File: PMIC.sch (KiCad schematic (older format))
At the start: 44 parts

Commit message: started working on implementing i.MX7 core into base schematic
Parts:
- removed D?: 1N5819HW-7-F, symbol SCHOTTKY
- removed U?: PF3000, symbol PF3000
- added BT?: Battery_Cell, symbol Battery_Cell
- added C? (x12): 22u, symbol C
- added D?: D_Schottky, symbol D_Schottky
- added R? (x4): 0R, symbol R
- added R?: 470R, symbol R
- added U?: PF3000, symbol PF3000
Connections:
- net labels added: DDR_VREF, NVCC_1V8, NVCC_DRAM, SW1AOUT, SW1BOUT, SW2OUT, SW3OUT, SWBSTOUT, VLDO1_1V8, VLDO2_1V5, VLDO3_3V3, VLDO4_2V8, VSNVS
- wire segments 152 -> 199
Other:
- moved on the sheet: C?

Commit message: fixed message telling to rescue PF3000 symbol while opening the schematic
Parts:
- removed U?: PF3000, symbol PF3000
- added U?: PF3000, symbol PF3000
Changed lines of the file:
@@
 EESchema Schematic File Version 2
-LIBS:3210retro-rescue
 LIBS:power
 LIBS:device
@@
 $Comp
 L PF3000 U?
-U 1 1 593FB77D
+U 1 1 59405399
 P 9450 2550
 F 0 "U?" H 9400 2887 60  0000 C CNN
 F 1 "PF3000" H 9400 2781 60  0000 C CNN
-F 2 "" H 100 -1950 60  0001 C CNN
-F 3 "" H 100 -1950 60  0001 C CNN
+F 2 "" H 50  -2400 60  0001 C CNN
+F 3 "" H 50  -2400 60  0001 C CNN
 	1    9450 2550
 	1    0    0    -1

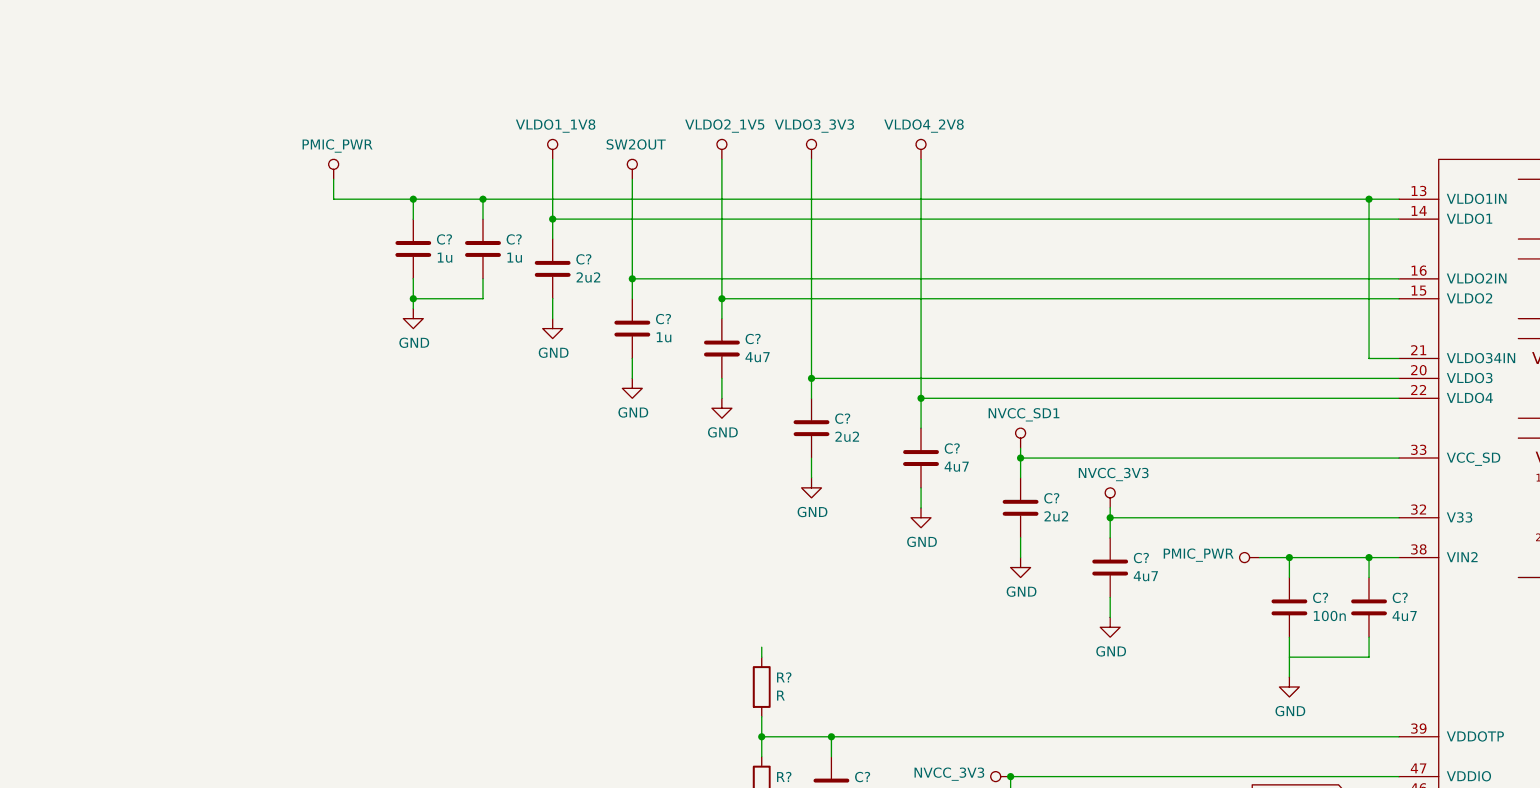
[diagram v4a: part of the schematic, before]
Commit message: Connected WIFI subsheet with ESP8266 and WL1807MOD to SD2 Connected WL1807MOD Bluetoth UART to UART3 Connected A7 Module AT UART to UART6 Connected A7 GPS UART to UART5 Connected A7 HS download to UART7 Connected debug pins to UART1 Connected debug pins to UART2 Added CPU_PWR subsheet to connect power rails to i.MX7 A7 UARTs are routed through level shifter to get from 2.8V to 3.3V All the sheets should be on A3 size now Externel USB is connected to USB_OTG1 Board power sheet is cleared out. Only 4V booster is needed.
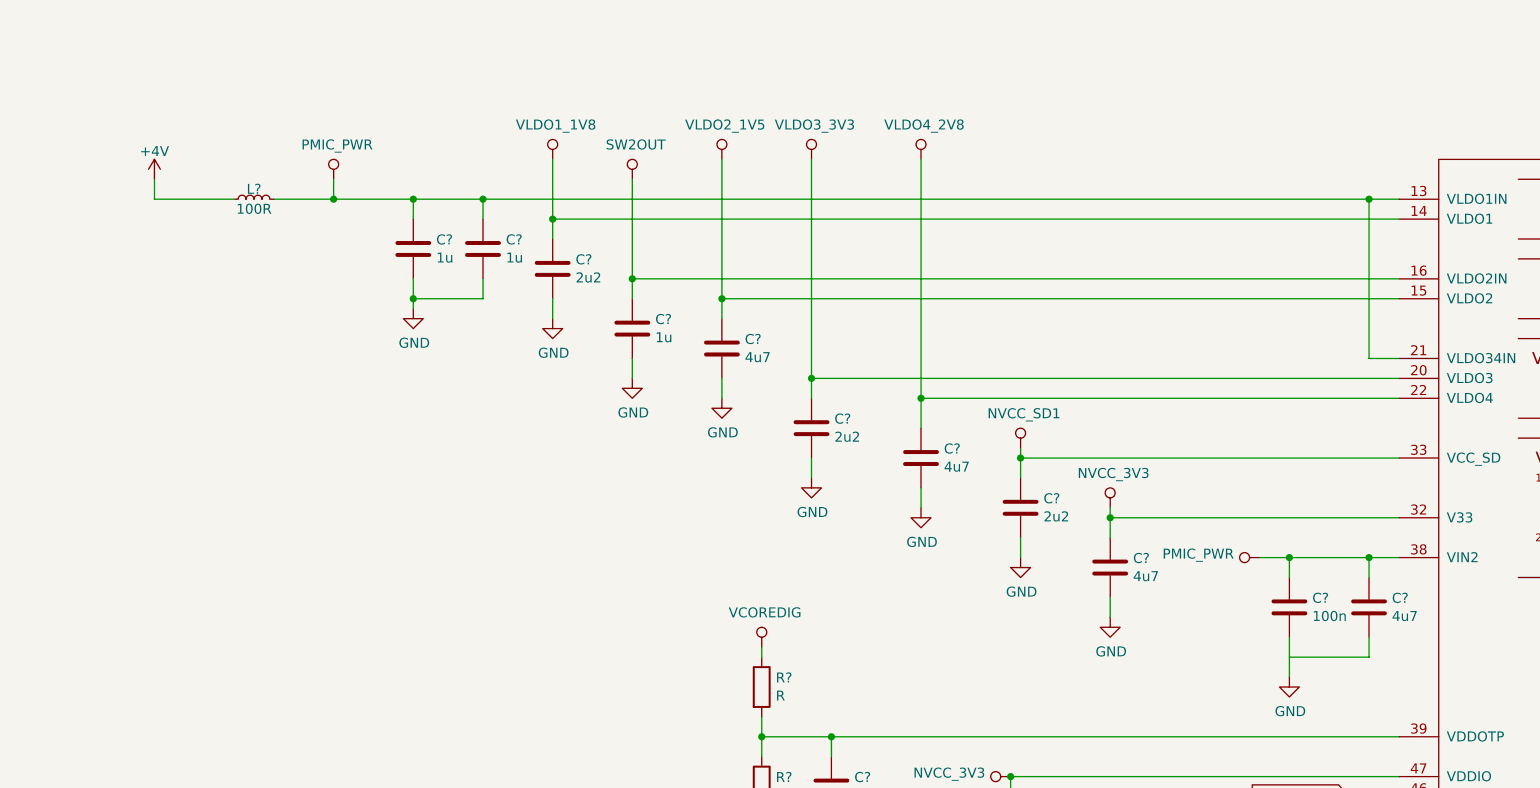
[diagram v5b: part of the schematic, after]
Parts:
- added L?: 100R, Resistors_SMD:R_0603, symbol L_Small
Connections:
- net labels added: +4V, VCOREDIG
- wire segments 199 -> 201
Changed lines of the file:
@@
 LIBS:emif06-msd02c3
 LIBS:mtfc8gacaeam-1m_wt
+LIBS:sn74avc2t244
 LIBS:3210retro-cache
 EELAYER 25 0
@@
 $Descr A3 16535 11693
 encoding utf-8
-Sheet 10 11
+Sheet 10 12
 Title "Nokia 3210 Retrofit"
-Date ""
+Date "2017-06-15"
 Rev "2"
 Comp "www.kurzschluss-blog.de"
-Comment1 ""
+Comment1 "Retrofitting board for Nokia 3210 mobile phone"
 Comment2 ""
 Comment3 ""
@@
 	2600 2500 2600 2600
 Wire Wire Line
-	2600 2600 7950 2600
+	2300 2600 7950 2600
 Connection ~ 3000 2600
 Connection ~ 3350 2600
@@
 	1    0    0    -1
 $EndComp
+$Comp
+L +4V #PWR?
+U 1 1 594861DD
+P 1700 2500
+F 0 "#PWR?" H 1700 2350 50  0001 C CNN
+F 1 "+4V" H 1700 2640 50  0000 C CNN
+F 2 "" H 1700 2500 50  0000 C CNN
+F 3 "" H 1700 2500 50  0000 C CNN
+	1    1700 2500
+	1    0    0    -1
+$EndComp
+$Comp
+L L_Small L?
+U 1 1 59487604
+P 2200 2600
+F 0 "L?" V 2250 2600 50  0000 C CNN
+F 1 "100R" V 2150 2600 50  0000 C CNN
+F 2 "Resistors_SMD:R_0603" H 2200 2600 50  0001 C CNN
+F 3 "" H 2200 2600 50  0000 C CNN
+	1    2200 2600
+	0    1    -1   0
+$EndComp
+Connection ~ 2600 2600
+Wire Wire Line
+	2100 2600 1700 2600
+Wire Wire Line
+	1700 2600 1700 2500
+$Comp
+L VCOREDIG #PWR?
+U 1 1 59487D09
+P 4750 4850
+F 0 "#PWR?" H 450 -600 50  0001 C CNN
+F 1 "VCOREDIG" H 4767 5023 50  0000 C CNN
+F 2 "" H 450 -450 50  0001 C CNN
+F 3 "" H 450 -450 50  0001 C CNN
+	1    4750 4850
+	1    0    0    -1
+$EndComp

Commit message: renamed USB.sch to USB_IMU.sch added LSM9DS1 IMU to USB_IMU.sch and connected I2C2 bus shuffeld stuff around to make MCU.sch less crammed
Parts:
- removed BT?: Battery_Cell, symbol Battery_Cell
- added BT?: Battery, symbol Battery
- L? (x5): symbol L_Core_Ferrite_Small -> L_Small
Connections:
- wire segments 201 -> 265

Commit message: modified adui circuit
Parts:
- removed BT?: Battery, symbol Battery
- added BT?: LI_BAT, symbol LI_BAT
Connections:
- net GND: now also BT?.2
- net at R?.1: now also BT?.1
